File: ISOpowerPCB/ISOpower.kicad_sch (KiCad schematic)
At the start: 24 parts, among them J1 XT60_connector_DC_60A_male, J21 24vTerminal, J22 12vTerminal, J23 5vTerminal, J24 dio_spare, J25 adc_spare, J26 USB_5v, J27 pwr_ctls, J28 MCU_DIO_A, J29 sensor_op, J30 MCU_ADC, J31 main_pwr, J32 MCU_PWR, J33 MCU_DIO_B, J34 O/P_ctls, Q1 IRF5305_PBF

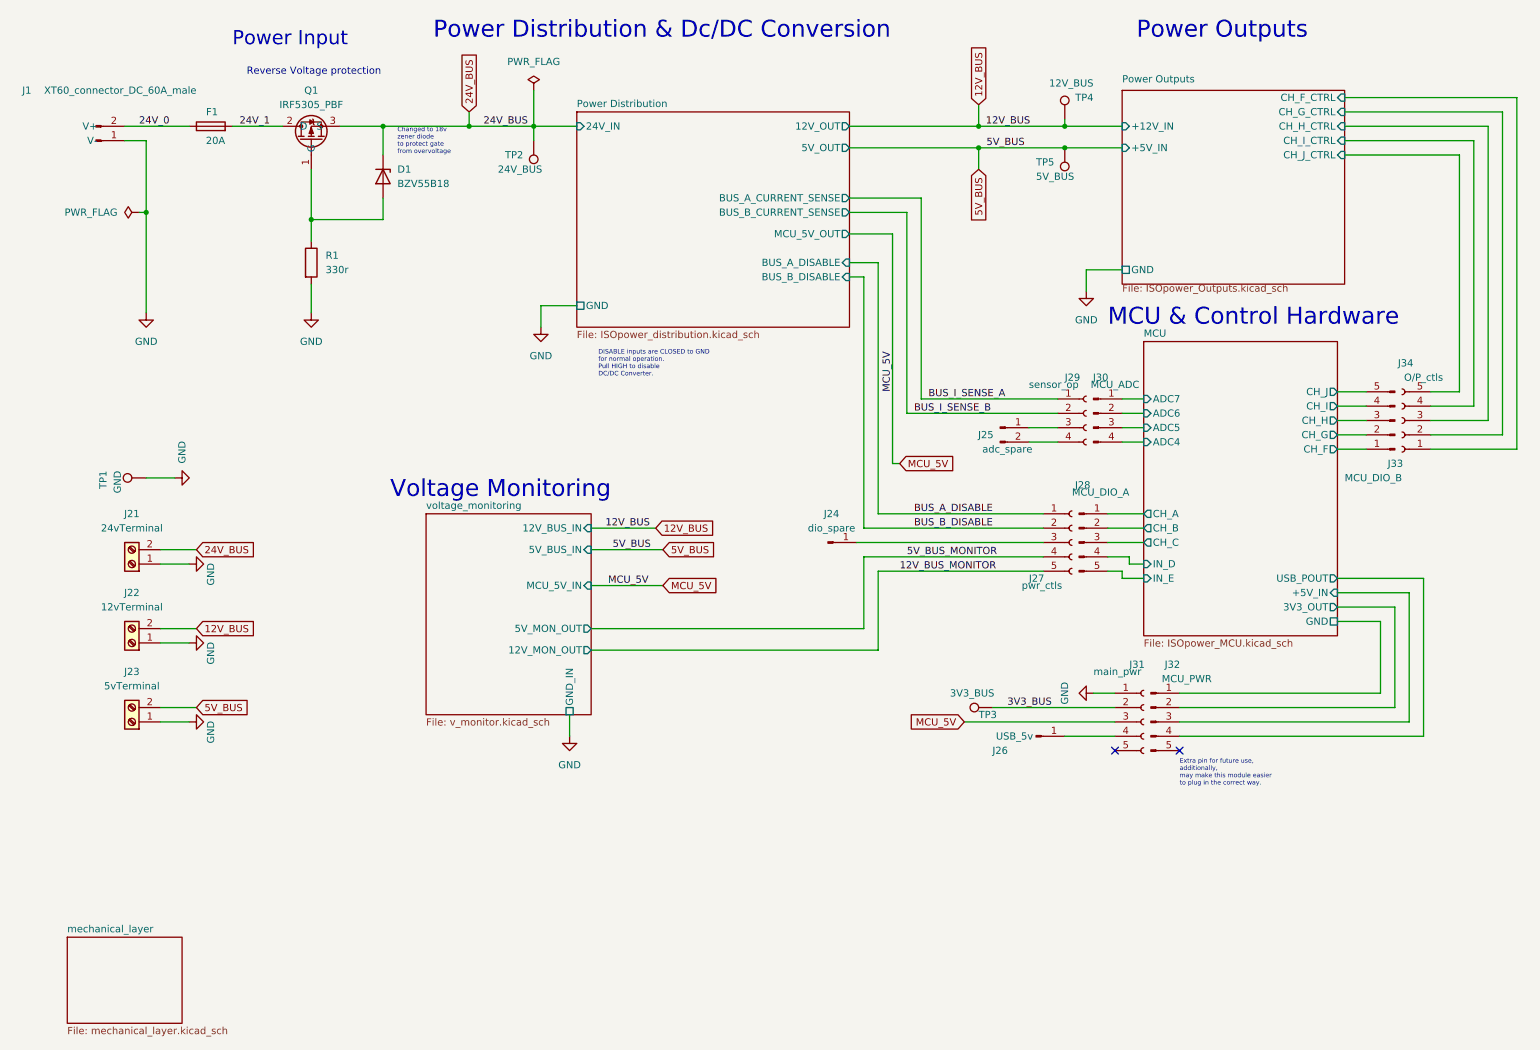
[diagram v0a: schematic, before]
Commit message: Components placed V1.0
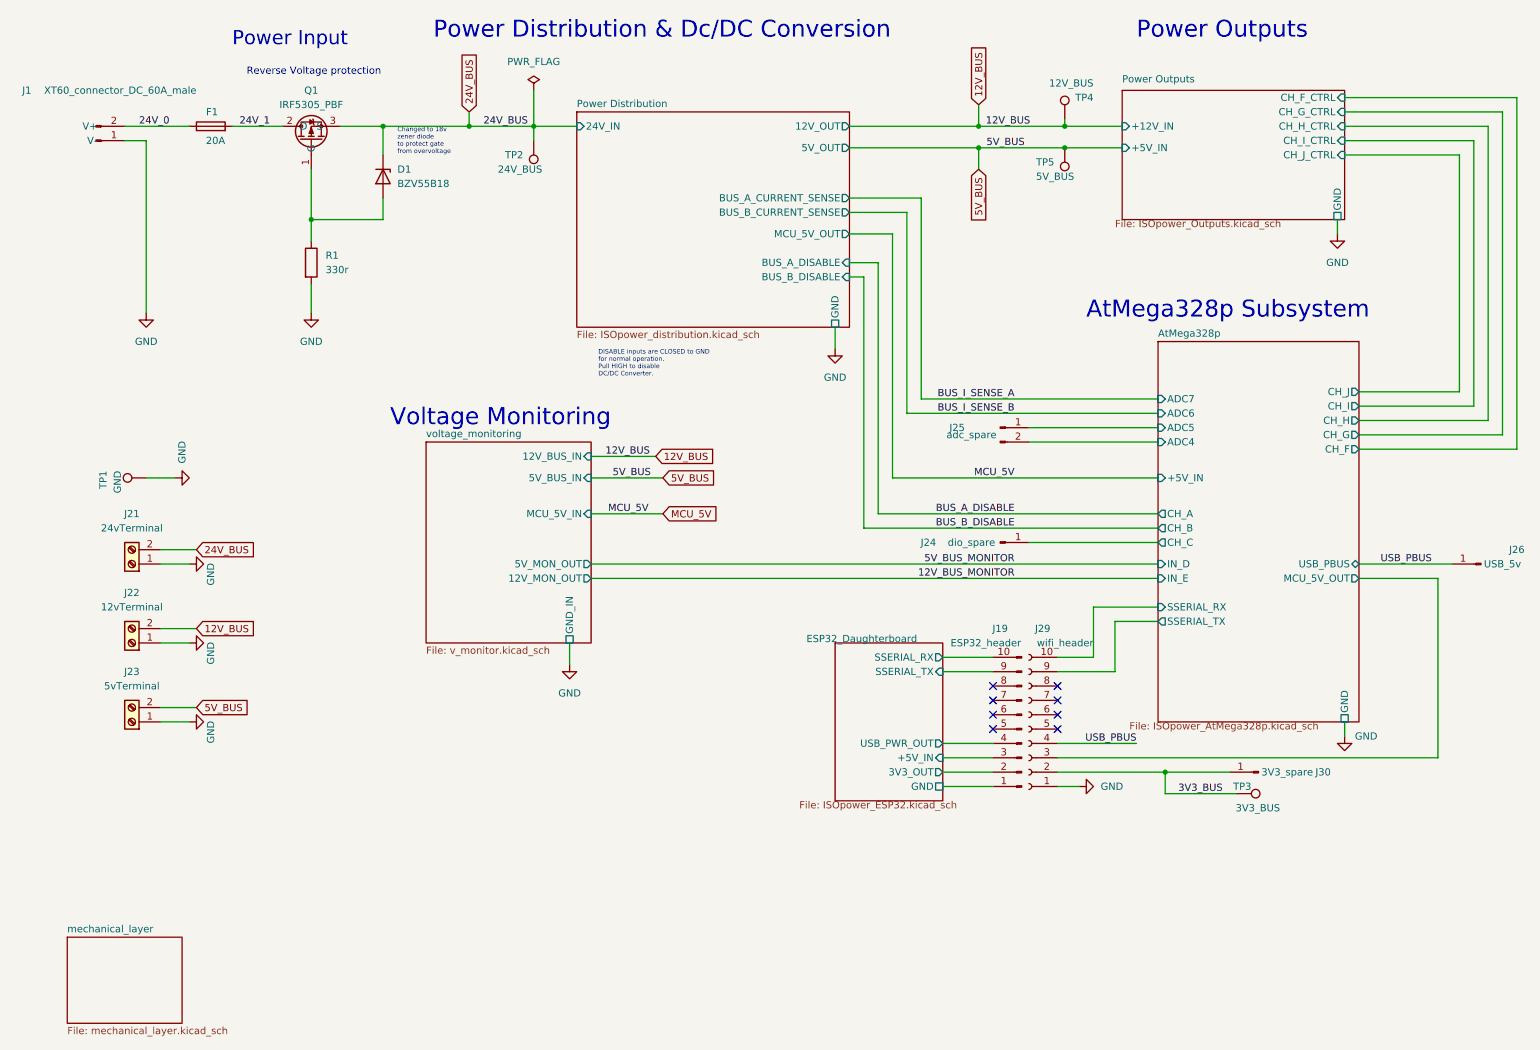
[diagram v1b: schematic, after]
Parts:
- removed J27: pwr_ctls, Connector_PinSocket_1.27mm:PinSocket_1x05_P1.27mm_Vertical, symbol 000_Pin_Headers_Immo:Conn_01x05_Female
- removed J28: MCU_DIO_A, Connector_PinHeader_1.27mm:PinHeader_1x05_P1.27mm_Vertical, symbol 000_Pin_Headers_Immo:Conn_01x05_Male
- removed J29: sensor_op, Connector_PinSocket_1.27mm:PinSocket_1x04_P1.27mm_Vertical, symbol 000_Pin_Headers_Immo:Conn_01x04_Female
- removed J30: MCU_ADC, Connector_PinHeader_1.27mm:PinHeader_1x04_P1.27mm_Vertical, symbol 000_Pin_Headers_Immo:Conn_01x04_Male
- removed J31: main_pwr, Connector_PinSocket_1.27mm:PinSocket_1x05_P1.27mm_Vertical, symbol 000_Pin_Headers_Immo:Conn_01x05_Female
- removed J32: MCU_PWR, Connector_PinHeader_1.27mm:PinHeader_1x05_P1.27mm_Vertical, symbol 000_Pin_Headers_Immo:Conn_01x05_Male
- removed J33: MCU_DIO_B, Connector_PinHeader_1.27mm:PinHeader_1x05_P1.27mm_Vertical, symbol 000_Pin_Headers_Immo:Conn_01x05_Male
- removed J34: O/P_ctls, Connector_PinSocket_1.27mm:PinSocket_1x05_P1.27mm_Vertical, symbol 000_Pin_Headers_Immo:Conn_01x05_Female
- added J19: ESP32_header, Connector_PinHeader_1.27mm:PinHeader_1x10_P1.27mm_Vertical, symbol Connector:Conn_01x10_Male
- added J29: wifi_header, Connector_PinSocket_1.27mm:PinSocket_1x10_P1.27mm_Vertical, symbol Connector:Conn_01x10_Female
- added J30: 3V3_spare, Connector_PinHeader_1.27mm:PinHeader_1x01_P1.27mm_Vertical, symbol 000_Pin_Headers_Immo:Conn_01x01_Male
- J1: footprint Connector_AMASS:AMASS_XT60-M_1x02_P7.20mm_Vertical -> Connector_AMASS:AMASS_XT60PW-M
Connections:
- net 3V3_BUS: now also J29.2 (Pin_2), J30.1 (Pin_1)
- net GND: now also J29.1 (Pin_1)
- net ESP32_Daughterboard/+5V_IN: now also J19.3 (Pin_3)
- net ESP32_Daughterboard/3V3_OUT: now also J19.2 (Pin_2)
- net ESP32_Daughterboard/GND: now also J19.1 (Pin_1)
- net USB_PBUS: now reaches J26.1 (Pin_1)
- net USB_PBUS: now also J29.4 (Pin_4)
- net AtMega328p/ADC5: now reaches J25.1 (Pin_1)
- net AtMega328p/ADC4: now reaches J25.2 (Pin_2)
- net AtMega328p/CH_C: now reaches J24.1 (Pin_1)
- new net AtMega328p/MCU_5V_OUT: J29.3 (Pin_3)
- new net AtMega328p/SSERIAL_RX: J29.10 (Pin_10)
- new net AtMega328p/SSERIAL_TX: J29.9 (Pin_9)
- new net ESP32_Daughterboard/SSERIAL_RX: J19.10 (Pin_10)
- new net ESP32_Daughterboard/SSERIAL_TX: J19.9 (Pin_9)
- new net ESP32_Daughterboard/USB_PWR_OUT: J19.4 (Pin_4)
- no-connect marks 2 -> 8
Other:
- sheet MCU renamed ESP32_Daughterboard
- added sheet AtMega328p (ISOpower_AtMega328p.kicad_sch)
- sheet ESP32_Daughterboard: file ISOpower_MCU.kicad_sch -> ISOpower_ESP32.kicad_sch
- sheet ESP32_Daughterboard ports: added SSERIAL_RX, SSERIAL_TX, USB_PWR_OUT; removed ADC4, ADC5, ADC6, ADC7, CH_A, CH_B, CH_C, CH_F, CH_G, CH_H, CH_I, CH_J, IN_D, IN_E, USB_POUT
- note added: "AtMega328p Subsystem"
- note removed: "Extra pin for future use, additionally, may make this module easier to plug in the correct way."
- note removed: "MCU & Control Hardware"
- moved on the sheet: J24, J26, TP3

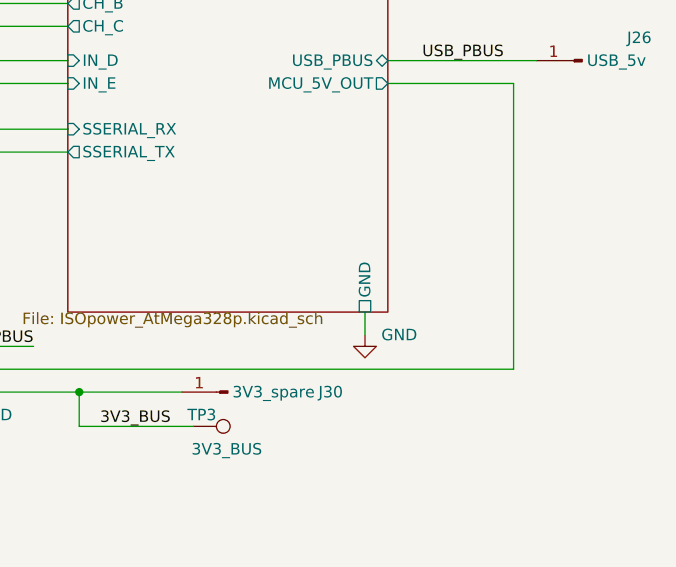
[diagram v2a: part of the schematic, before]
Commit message: PCB layout completed.
Screenshots added to media folder
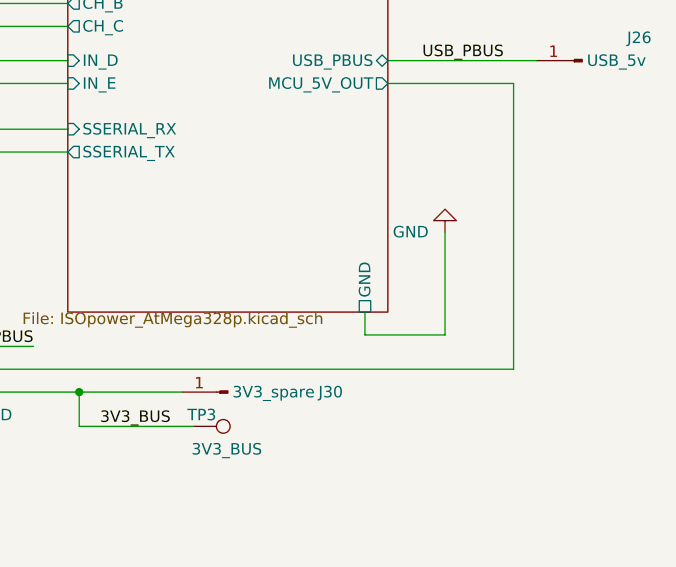
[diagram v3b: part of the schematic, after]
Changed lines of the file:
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@@
+    (stroke (width 0) (type default) (color 0 0 0 0))
+  )
+  (wire (pts (xy 243.84 142.24) (xy 243.84 139.7))
     (stroke (width 0) (type default) (color 0 0 0 0))
   )
@@
     (stroke (width 0) (type default) (color 0 0 0 0))
   )
+  (wire (pts (xy 252.73 130.81) (xy 252.73 142.24))
+    (stroke (width 0) (type default) (color 0 0 0 0))
+  )
   (wire (pts (xy 73.66 46.99) (xy 73.66 50.8))
     (stroke (width 0) (type default) (color 0 0 0 0))
@@
     (stroke (width 0) (type default) (color 0 0 0 0))
   )
+  (wire (pts (xy 243.84 142.24) (xy 252.73 142.24))
+    (stroke (width 0) (type default) (color 0 0 0 0))
+  )
   (wire (pts (xy 193.04 148.59) (xy 212.09 148.59))
     (stroke (width 0) (type default) (color 0 0 0 0))
@@
   )
   (wire (pts (xy 34.29 111.76) (xy 39.37 111.76))
-    (stroke (width 0) (type default) (color 0 0 0 0))
-  )
-  (wire (pts (xy 243.84 139.7) (xy 243.84 142.24))
     (stroke (width 0) (type default) (color 0 0 0 0))
   )
@@
     (pin "1")
   )
-  (symbol (lib_id "power:GND") (at 243.84 142.24 0) (unit 1)
-    (in_bom yes) (on_board yes)
-    (property "Reference" "#PWR07" (id 0) (at 243.84 148.59 0)
-      (effects (font (size 1.27 1.27)) hide)
-    )
-    (property "Value" "GND" (id 1) (at 247.65 142.24 0))
-    (property "Footprint" "" (id 2) (at 243.84 142.24 0)
-      (effects (font (size 1.27 1.27)) hide)
-    )
-    (property "Datasheet" "" (id 3) (at 243.84 142.24 0)
+  (symbol (lib_id "power:GND") (at 252.73 130.81 180) (unit 1)
+    (in_bom yes) (on_board yes)
+    (property "Reference" "#PWR07" (id 0) (at 252.73 124.46 0)
+      (effects (font (size 1.27 1.27)) hide)
+    )
+    (property "Value" "GND" (id 1) (at 248.92 130.81 0))
+    (property "Footprint" "" (id 2) (at 252.73 130.81 0)
+      (effects (font (size 1.27 1.27)) hide)
+    )
+    (property "Datasheet" "" (id 3) (at 252.73 130.81 0)
       (effects (font (size 1.27 1.27)) hide)
     )
@@
       (reference "N2") (unit 1) (value "Net_Tie") (footprint "NetTie:NetTie-2_SMD_Pad0.5mm")
     )
+    (path "/f9ad6110-c54c-46dc-af11-fdacac24e4c9/25ed1cf0-c8d2-4dff-976a-8c6ef9999bc8"
+      (reference "N3") (unit 1) (value "Net_Tie") (footprint "NetTie:NetTie-2_SMD_Pad0.5mm")
+    )
+    (path "/f811a9bf-1128-4bae-b7e5-2ff69e6cf287/0b2dd2a0-5914-4989-b40c-f863b28408f5"
+      (reference "N4") (unit 1) (value "Net_Tie") (footprint "NetTie:NetTie-2_SMD_Pad0.5mm")
+    )
     (path "/bd4eb304-3e85-4f2d-8568-e8105e1edb8e"

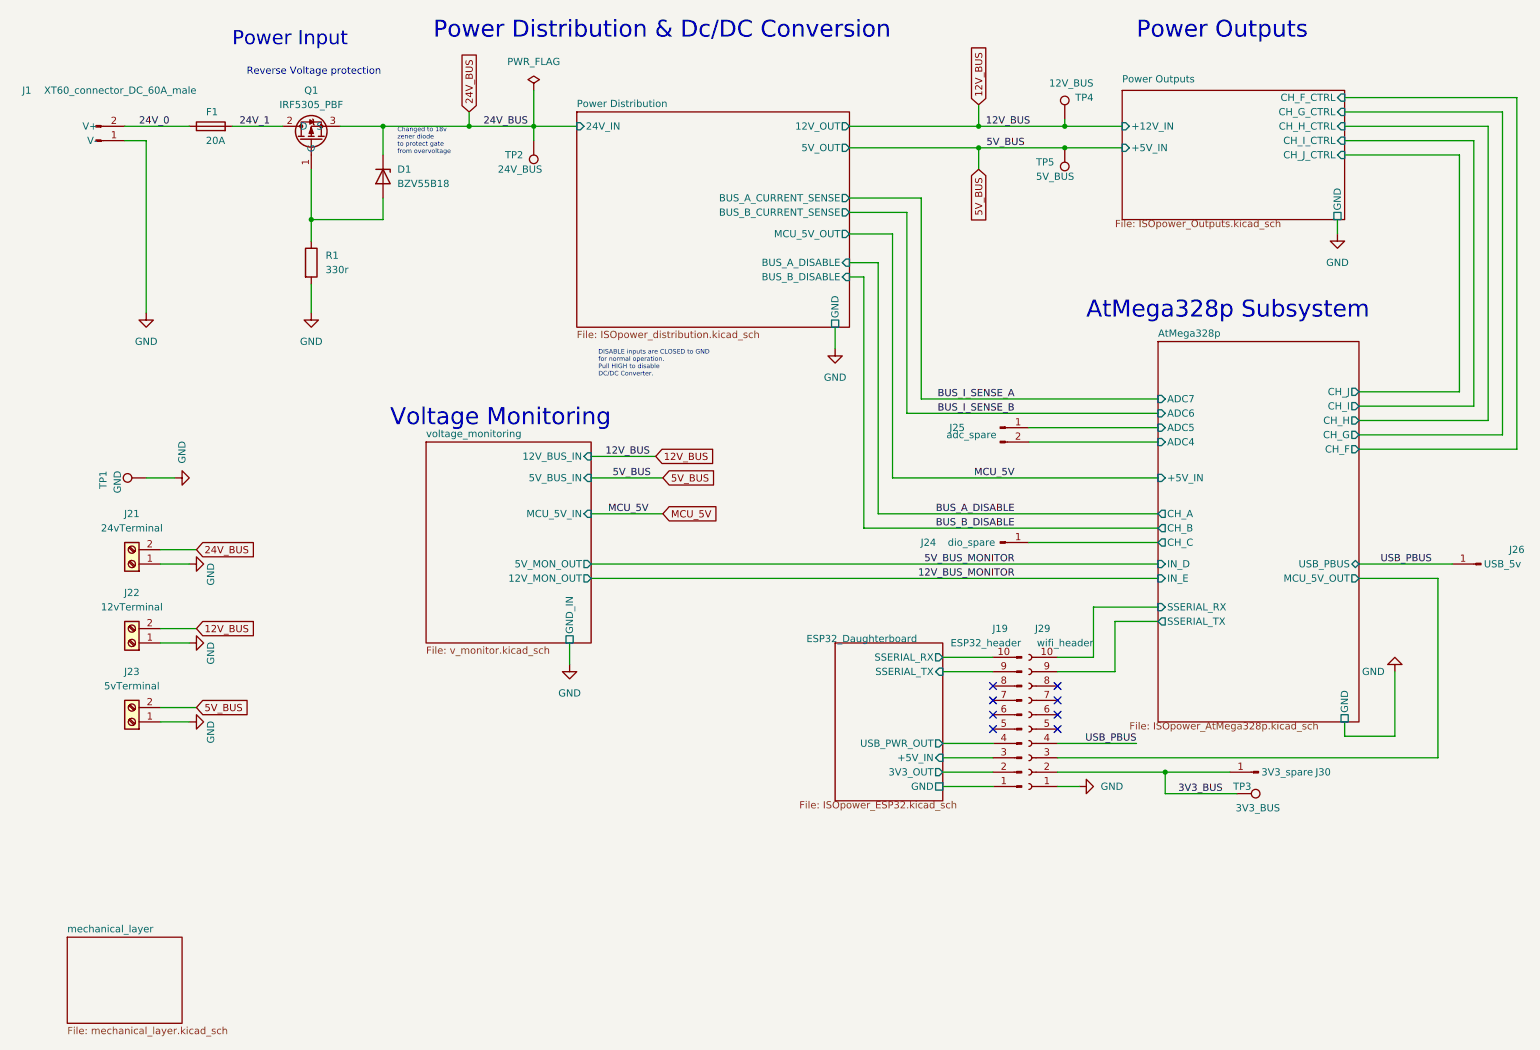
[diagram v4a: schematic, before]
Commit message: Replacing power bus RE current draw issue
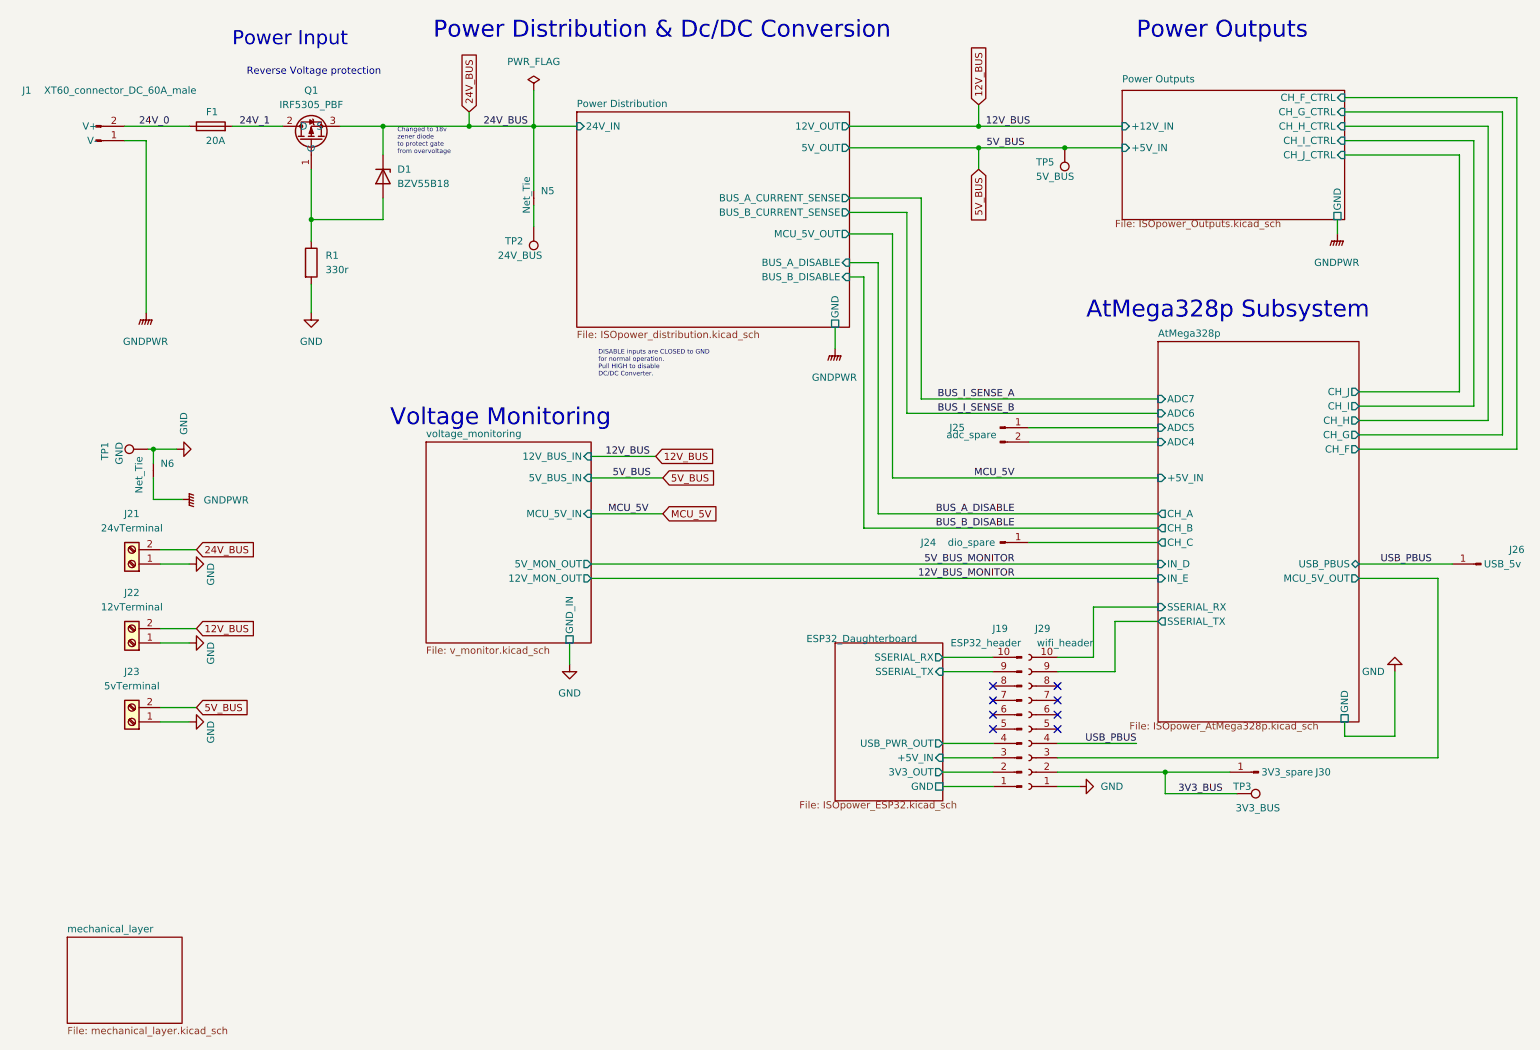
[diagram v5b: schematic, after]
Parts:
- removed TP4: 12V_BUS, TestPoint:TestPoint_Pad_D1.5mm, symbol Connector:TestPoint
- added N5, N6: Net_Tie, NetTie:NetTie-2_SMD_Pad0.5mm, symbol 000_Utility_Immo:Net_Tie
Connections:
- net 24V_BUS: now also N5.2 (C); no longer TP2.1
- net GND: now also N6.2 (C); no longer J1.1 (V-)
- new net: N5.1 (A), TP2.1
- new net GNDPWR: J1.1 (V-), N6.1 (A)
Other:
- moved on the sheet: TP1, TP2
